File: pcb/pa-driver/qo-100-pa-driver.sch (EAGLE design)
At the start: 45 parts, among them CON1 2EDG-2P-5.08MM, Q1 BLP9G0722-20G, U1 ADP7142AUJZ, U2 2450BP15E0100

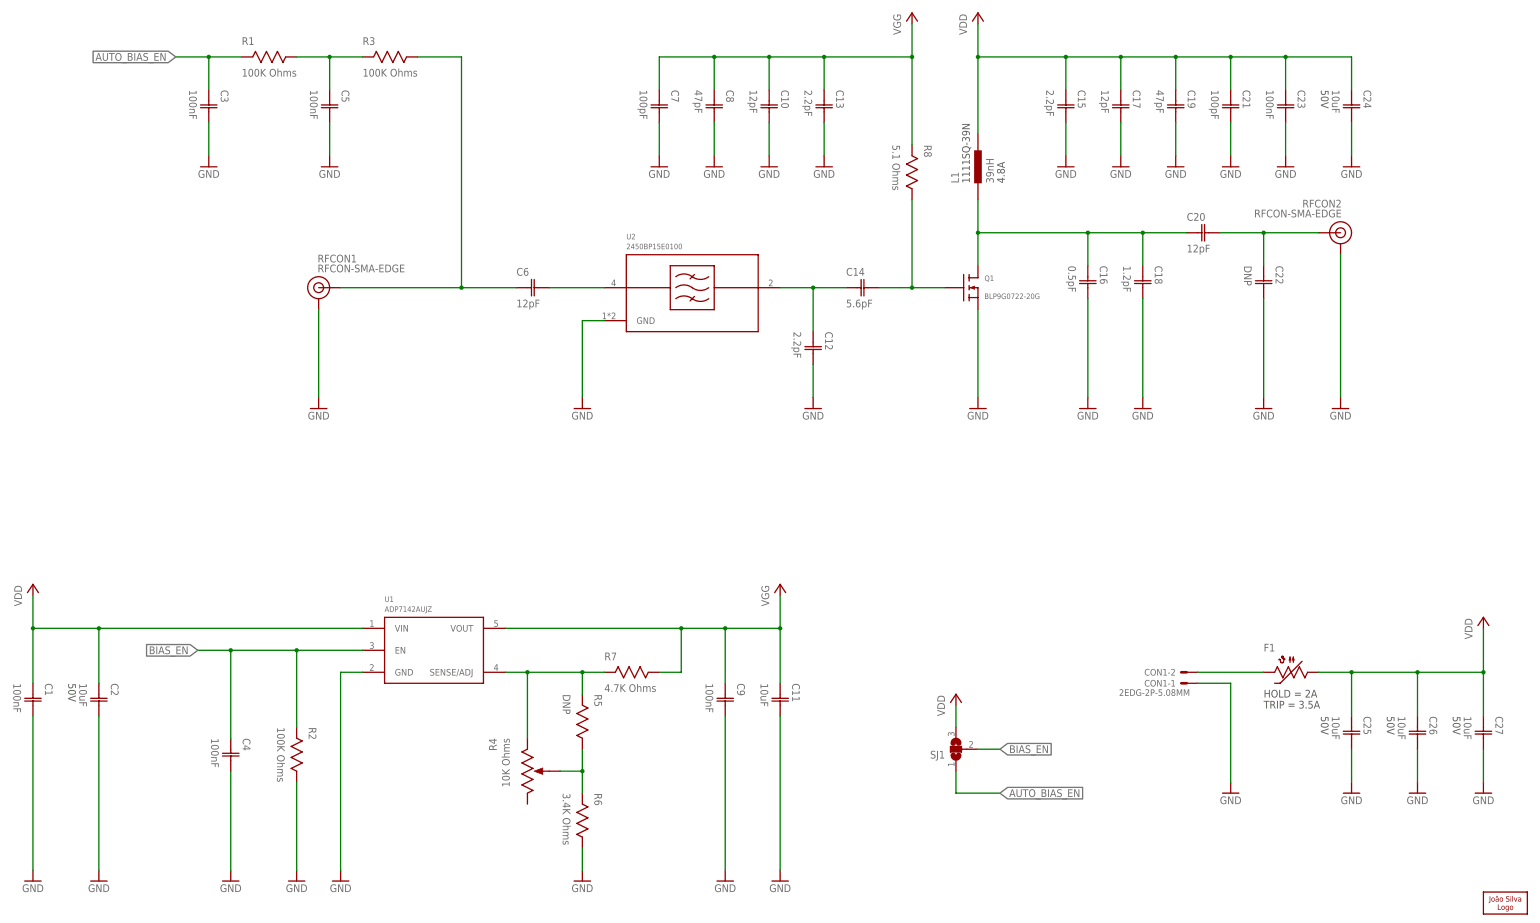
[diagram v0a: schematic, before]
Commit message: New PA driver design
Signed-off-by: João Silva <jgc3silva@gmail.com>
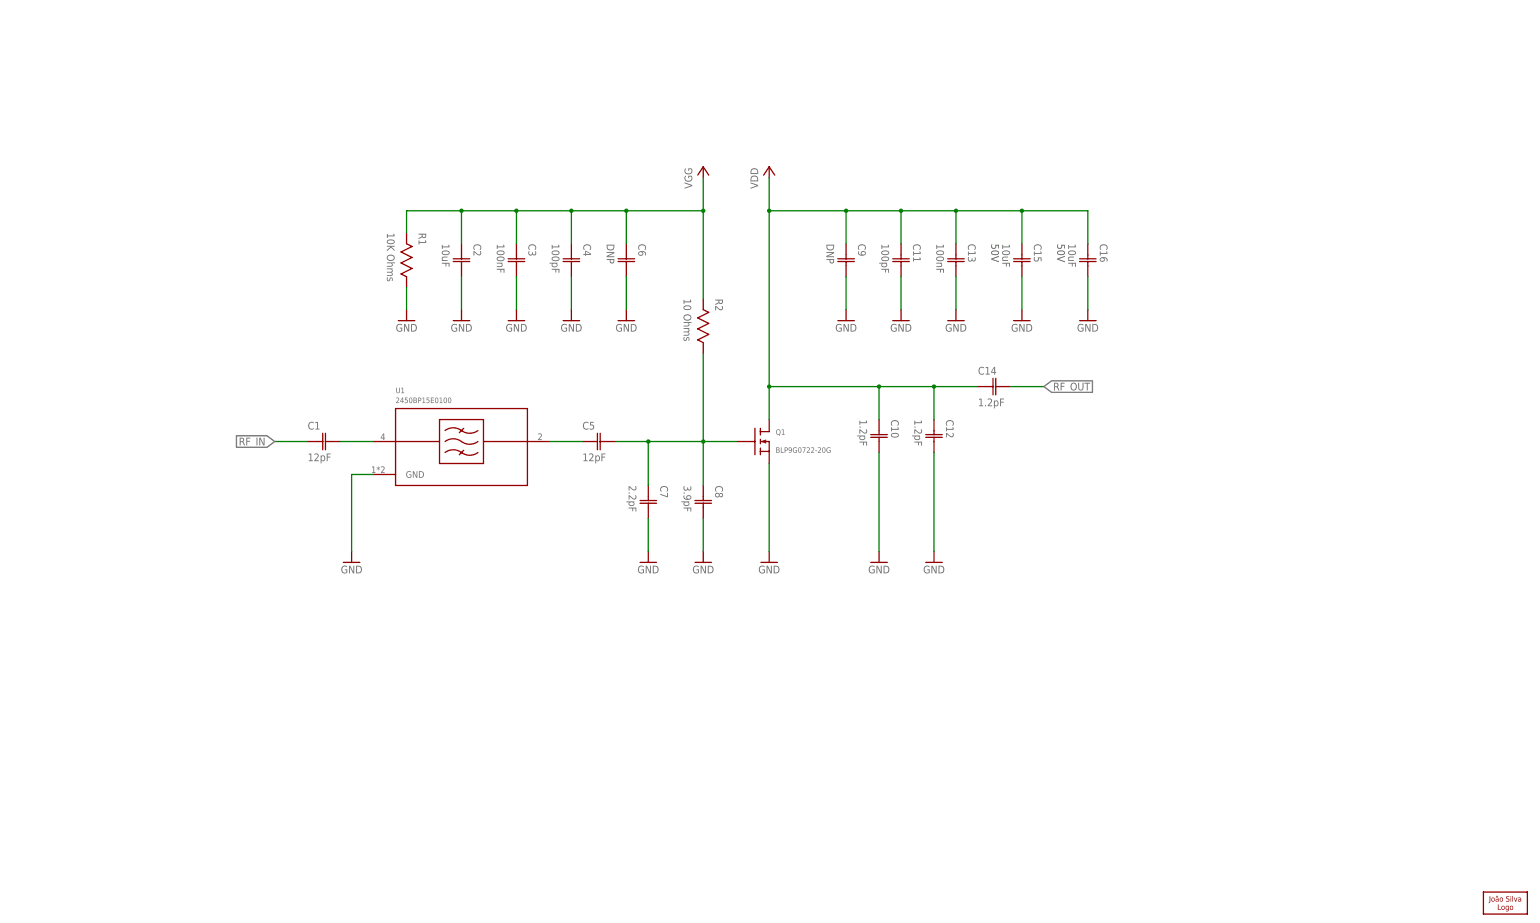
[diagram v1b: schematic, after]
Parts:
- removed C17, C20: 12pF, Capacitor:CAPACITOR-0603
- removed C18: 1.2pF, Capacitor:CAPACITOR-0603
- removed C19: 47pF, Capacitor:CAPACITOR-0603
- removed C21: 100pF, Capacitor:CAPACITOR-0603
- removed C22: DNP, Capacitor:CAPACITOR-0603
- removed C23: 100nF, Capacitor:CAPACITOR-0603
- removed C24, C25, C26, C27: 10uF, Capacitor:CAPACITOR-1206
- removed CON1: 2EDG-2P-5.08MM, Generic Connector:2EDG-2P-5.08MM
- removed F1: (no value), PTC Fuses:PTC1206
- removed L1: 39nH, Coilcraft:1111SQ-39N
- removed R3: 100K Ohms, Resistor:RESISTOR-0603
- removed R4: 10K Ohms, Potentiometer:POTENTIOMETER-SMD-3X3
- removed R5: DNP, Resistor:RESISTOR-0603
- removed R6: 3.4K Ohms, Resistor:RESISTOR-0603
- removed R7: 4.7K Ohms, Resistor:RESISTOR-0603
- removed R8: 5.1 Ohms, Resistor:RESISTOR-0603
- removed RFCON1, RFCON2: RFCON-SMA-EDGE, RF Connector:RFCON-SMA-EDGE
- removed SJ1: (no value), Solder Jumper:SJ2S
- removed U2: 2450BP15E0100, Generic Filter:2450BP15E0100
- C1, C5: value 100nF -> 12pF
- C10: value 12pF -> 1.2pF
- C11: value 10uF -> 100pF
- C12: value 2.2pF -> 1.2pF
- C13: value 2.2pF -> 100nF
- C14: value 5.6pF -> 1.2pF
- C15: value 2.2pF -> 10uF; device Capacitor:CAPACITOR-0603 -> Capacitor:CAPACITOR-1206; VOLTAGE (none) -> 50V
- C16: value 0.5pF -> 10uF; device Capacitor:CAPACITOR-0603 -> Capacitor:CAPACITOR-1206; VOLTAGE (none) -> 50V
- C2: device Capacitor:CAPACITOR-1206 -> Capacitor:CAPACITOR-0603; VOLTAGE 50V -> (none)
- C4: value 100nF -> 100pF
- C6: value 12pF -> DNP
- C7: value 100pF -> 2.2pF
- C8: value 47pF -> 3.9pF
- C9: value 100nF -> DNP
- LOGO1: value JS-10MM -> JS-5MM; device Silkscreen:JS-10MM -> Silkscreen:JS-5MM
- R1: value 100K Ohms -> 10K Ohms
- R2: value 100K Ohms -> 10 Ohms
- U1: value ADP7142AUJZ -> 2450BP15E0100; device Analog Devices:ADP7142AUJZ -> Generic Filter:2450BP15E0100
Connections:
- removed net AUTO_BIAS_EN: C3.C1, R1.2, SJ1.1
- removed net BIAS_EN: C4.C1, R2.2, SJ1.2, U1.EN
- removed net N$1: CON1-2.S, F1.2
- removed net N$12: C6.C1, R3.1, RFCON1.SIGNAL
- removed net N$3: C16.C1, C18.C1, C20.C1, L1.1, Q1.D
- removed net N$4: C20.C2, C22.C1, RFCON2.SIGNAL
- removed net N$7: C5.C1, R1.1, R3.2
- removed net N$8: R4.CCW, R5.2, R7.2, U1.SENSE/ADJ
- removed net N$9: R4.WIPER, R5.1, R6.2
- new net RF_IN: C1.C1
- new net RF_OUT: C14.C2
- net GND: now also C6.C2, R1.1; no longer C1.C2, C17.C2, C18.C2, C19.C2, C21.C2, C22.C2, C23.C2, C24.C2, C25.C2, C26.C2, C27.C2, C5.C2, CON1-1.S, R2.1, R6.1, RFCON1.GND, RFCON2.GND, U2.GND
- net N$2: now also C5.C2, C7.C1, C8.C1, R2.1; no longer C14.C2, R8.1
- net N$5: now also C5.C1, U1.RFOUT; no longer C12.C1, C14.C1, U2.RFOUT
- net N$6: now also C1.C2, U1.RFIN; no longer C6.C2, U2.RFIN
- net VDD: now also C10.C1, C11.C1, C12.C1, C13.C1, C14.C1, C16.C1, C9.C1, Q1.D; no longer C1.C1, C17.C1, C19.C1, C2.C1, C21.C1, C23.C1, C24.C1, C25.C1, C26.C1, C27.C1, F1.1, L1.2, SJ1.3, U1.VIN
- net VGG: now also C2.C1, C3.C1, C4.C1, C6.C1, R1.2, R2.2; no longer C10.C1, C11.C1, C13.C1, C7.C1, C8.C1, C9.C1, R7.1, R8.2, U1.VOUT
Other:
- note removed: "Gate bias adjust"
- moved on the sheet: C1, C10, C11, C12, C13, C14, C15, C16, C2, C3, C4, C5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

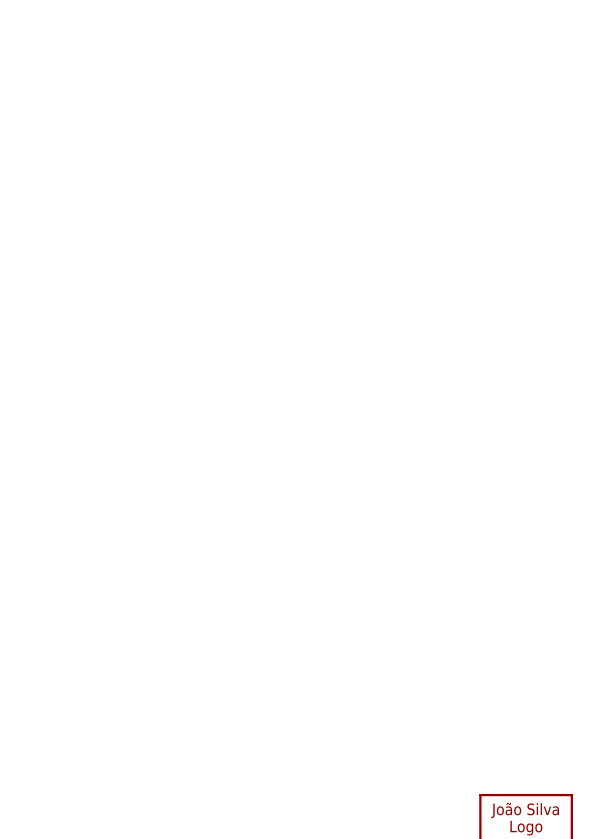
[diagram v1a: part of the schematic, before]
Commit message: Add thermal sensing diode to PA Driver
Signed-off-by: João Silva <jgc3silva@gmail.com>
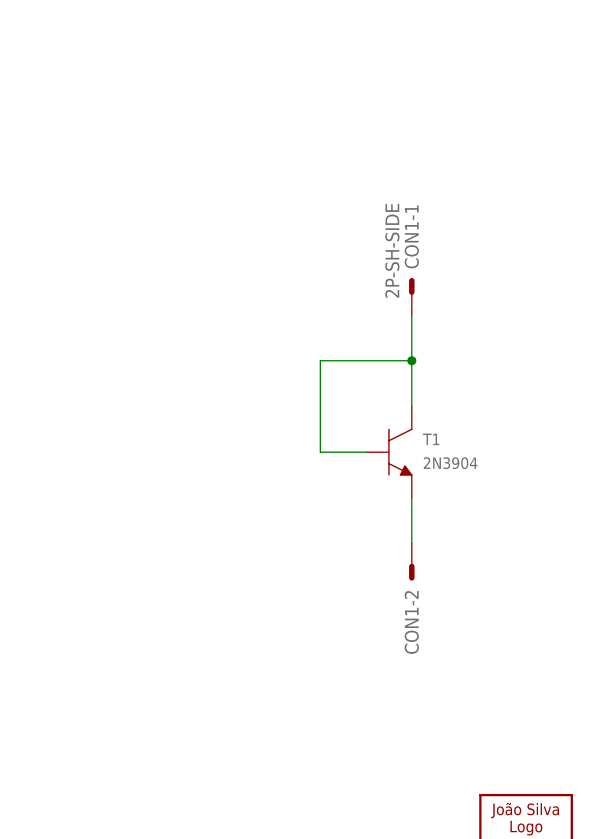
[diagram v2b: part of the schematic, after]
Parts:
- added CON1: 2P-SH-SIDE, JST:2P-SH-SIDE
- added T1: 2N3904, Generic BJT:2N3904
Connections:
- new net N$1: CON1-2.S, T1.E
- new net N$3: CON1-1.S, T1.B, T1.C
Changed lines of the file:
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@@
 <part name="C2" library="Capacitor" deviceset="CAPACITOR" device="-0603" value="10uF"/>
 <part name="GND7" library="Supply Symbol" deviceset="GND" device=""/>
+<part name="T1" library="Generic BJT" deviceset="2N3904" device=""/>
+<part name="CON1" library="JST" deviceset="2P" device="-SH-SIDE"/>
 </parts>
 <sheets>
@@
 <instance part="GND7" gate="G$1" x="132.08" y="160.02" smashed="yes">
 <attribute name="VALUE" x="132.08" y="154.94" size="1.778" layer="96" align="bottom-center"/>
+</instance>
+<instance part="T1" gate="G$1" x="358.14" y="63.5" smashed="yes">
+<attribute name="NAME" x="361.9246" y="64.2874" size="1.27" layer="95"/>
+<attribute name="VALUE" x="361.8992" y="61.6458" size="1.27" layer="96"/>
+</instance>
+<instance part="CON1" gate="-1" x="360.68" y="81.28" smashed="yes" rot="R90">
+<attribute name="NAME" x="361.442" y="83.82" size="1.524" layer="95" rot="R90"/>
+<attribute name="VALUE" x="359.283" y="80.518" size="1.524" layer="96" rot="R90"/>
+</instance>
+<instance part="CON1" gate="-2" x="360.68" y="50.8" smashed="yes" rot="R270">
+<attribute name="NAME" x="359.918" y="48.26" size="1.524" layer="95" rot="R270"/>
 </instance>
 </instances>
@@
 </segment>
 </net>
+<net name="N$1" class="0">
+<segment>
+<pinref part="CON1" gate="-2" pin="S"/>
+<pinref part="T1" gate="G$1" pin="E"/>
+<wire x1="360.68" y1="53.34" x2="360.68" y2="58.42" width="0.1524" layer="91"/>
+</segment>
+</net>
+<net name="N$3" class="0">
+<segment>
+<pinref part="T1" gate="G$1" pin="B"/>
+<wire x1="355.6" y1="63.5" x2="350.52" y2="63.5" width="0.1524" layer="91"/>
+<wire x1="350.52" y1="63.5" x2="350.52" y2="73.66" width="0.1524" layer="91"/>
+<wire x1="350.52" y1="73.66" x2="360.68" y2="73.66" width="0.1524" layer="91"/>
+<pinref part="CON1" gate="-1" pin="S"/>
+<wire x1="360.68" y1="73.66" x2="360.68" y2="78.74" width="0.1524" layer="91"/>
+<pinref part="T1" gate="G$1" pin="C"/>
+<wire x1="360.68" y1="68.58" x2="360.68" y2="73.66" width="0.1524" layer="91"/>
+<junction x="360.68" y="73.66"/>
+</segment>
+</net>
